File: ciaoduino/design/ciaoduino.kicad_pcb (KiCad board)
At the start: 2 copper layers, 50.5 x 47.8 mm, 19 parts, among them P1 ICSP, P2 CONN_01X02, P3 USB_OTG, P4 CONN_01X06, P5 CONN_01X06, P6 CONN_01X04, P7 CONN_01X14, SW1 SW_PUSH, SW2 SW_PUSH, U2 ATmega32U4-AU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

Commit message: Rework layout.
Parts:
- added REF**: MountingHole_2.5mm, Mounting_Holes:MountingHole_2.5mm, F.Cu at (131.8, 65.8)
- moved P5 5.39 mm to (143.5, 96.5), turned to 270 degrees
- moved P4 5.29 mm to (161.3, 96.5), turned to 90 degrees
- moved P6 4.58 mm to (148.6, 96.5)
- moved P2 2.90 mm to (135.6, 66.8), turned to 90 degrees
- moved REF** 2.70 mm to (172.2, 65.8)
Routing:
- net usart_tx: track 24.9 -> 5.07 mm
- net usart_cts: track 28.3 -> 48.1 mm
- net SCLK: track 25.7 -> 31.2 mm
- net SS: track 29.3 -> 34.4 mm
- net SCL: track 21.3 -> 16.7 mm
- net SDA: track 22.0 -> 17.4 mm
- net GND: track 15.1 -> 16.7 mm
- net VCC: track 145.5 -> 144.5 mm
- net MOSI: track 24.4 -> 23.8 mm
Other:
- board size 50.5 x 47.8 mm -> 50.5 x 42.7 mm

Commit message: Rework layout.
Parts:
- removed REF** (x2): MountingHole_2.5mm, Mounting_Holes:MountingHole_2.5mm
- P4: footprint Pin_Headers:Pin_Header_Angled_1x06 -> Pin_Headers:Pin_Header_Straight_1x06
- SW2: footprint Buttons_Switches_SMD:SW_SPST_EVQP0 -> Buttons_Switches_SMD:SW_SPST_KMR2
- moved P1 41.3 mm to (172.6, 73.0), turned to 0 degrees
- moved SW1 7.19 mm to (164.1, 77.5)
- moved P2 7.08 mm to (128.8, 65.0), turned to 180 degrees
- moved SW2 6.10 mm to (164.2, 73.7)
- moved C3 2.56 mm to (140.2, 76.1), turned to 0 degrees
- moved P6 2.29 mm to (148.6, 98.8)
- moved R4 1.49 mm to (140.2, 72.5)
- moved P3 0.97 mm to (130.4, 75.8)
- moved R3 0.81 mm to (140.2, 74.3)
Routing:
- net VCC: track 144.5 -> 79.9 mm, vias 8 -> 6
- net SS: track 34.4 -> 0.00 mm
- net SCLK: track 31.2 -> 0.64 mm
- net MISO: track 29.6 -> 1.30 mm, vias 2 -> 0
- net MOSI: track 23.8 -> 1.52 mm, vias 1 -> 0
- net usart_cts: track 48.1 -> 28.3 mm
- net RESET: track 49.8 -> 35.6 mm
- net Net-(R2-Pad2): track 17.4 -> 6.26 mm
- net Net-(C3-Pad2): track 8.06 -> 0.00 mm
- net Net-(P3-Pad2): track 6.08 -> 0.24 mm
- net Net-(R4-Pad1): track 5.56 -> 0.00 mm
- net Net-(P3-Pad3): track 5.22 -> 0.00 mm
- net Net-(R3-Pad1): track 5.12 -> 0.00 mm
- net usart_tx: track 5.07 -> 0.00 mm
- net GND: track 16.7 -> 13.9 mm
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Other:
- board size 50.5 x 42.7 mm -> 59.1 x 42.7 mm

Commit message: ciaoduino: rework board.
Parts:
- added C4: C, Capacitors_SMD:C_0603_HandSoldering, F.Cu at (134.4, 63.8)
- added C5: C, Capacitors_SMD:C_0603_HandSoldering, F.Cu at (141.5, 67.8)
- added Q1: Q_NMOS_DGS, TO_SOT_Packages_SMD:SOT-23, F.Cu at (137.9, 67.6)
- added U1: MCP1754ST-5002E/MB, TO_SOT_Packages_SMD:SOT-323, F.Cu at (134.1, 65.8)
- moved R1 6.37 mm to (165.6, 81.3)
- moved P6 4.83 mm to (148.6, 94.0)
- moved C1 3.31 mm to (154.4, 84.8)
- moved C2 3.31 mm to (147.8, 84.8), turned to 90 degrees
- moved X1 2.79 mm to (151.1, 84.8)
- moved P4 2.54 mm to (161.3, 94.0)
- moved P5 2.54 mm to (143.5, 94.0)
- moved R2 0.57 mm to (162.1, 69.6), turned to 270 degrees
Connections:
- P2 pad 2: VCC -> Net-(C4-Pad2)
- P3 pad 1: (no net) -> VCCUSB
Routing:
- net usart_rts: track 38.6 -> 0.00 mm, vias 2 -> 0
- net RESET: track 35.6 -> 4.10 mm, vias 2 -> 0
- net usart_cts: track 28.3 -> 0.00 mm, vias 2 -> 0
- net usart_rx: track 25.1 -> 0.00 mm
- net SDA: track 19.7 -> 0.00 mm
- net SCL: track 19.0 -> 0.00 mm
- net Net-(C4-Pad2): track 0.00 -> 9.40 mm
- net Net-(C2-Pad1): track 14.8 -> 6.34 mm, vias 2 -> 0
- net Net-(C1-Pad1): track 11.5 -> 4.14 mm, vias 2 -> 0
- net Net-(R2-Pad2): track 6.26 -> 12.4 mm
- net GND: track 13.9 -> 17.8 mm
- net VCC: track 79.9 -> 77.0 mm, vias 6 -> 5
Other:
- board size 59.1 x 42.7 mm -> 59.2 x 35.1 mm

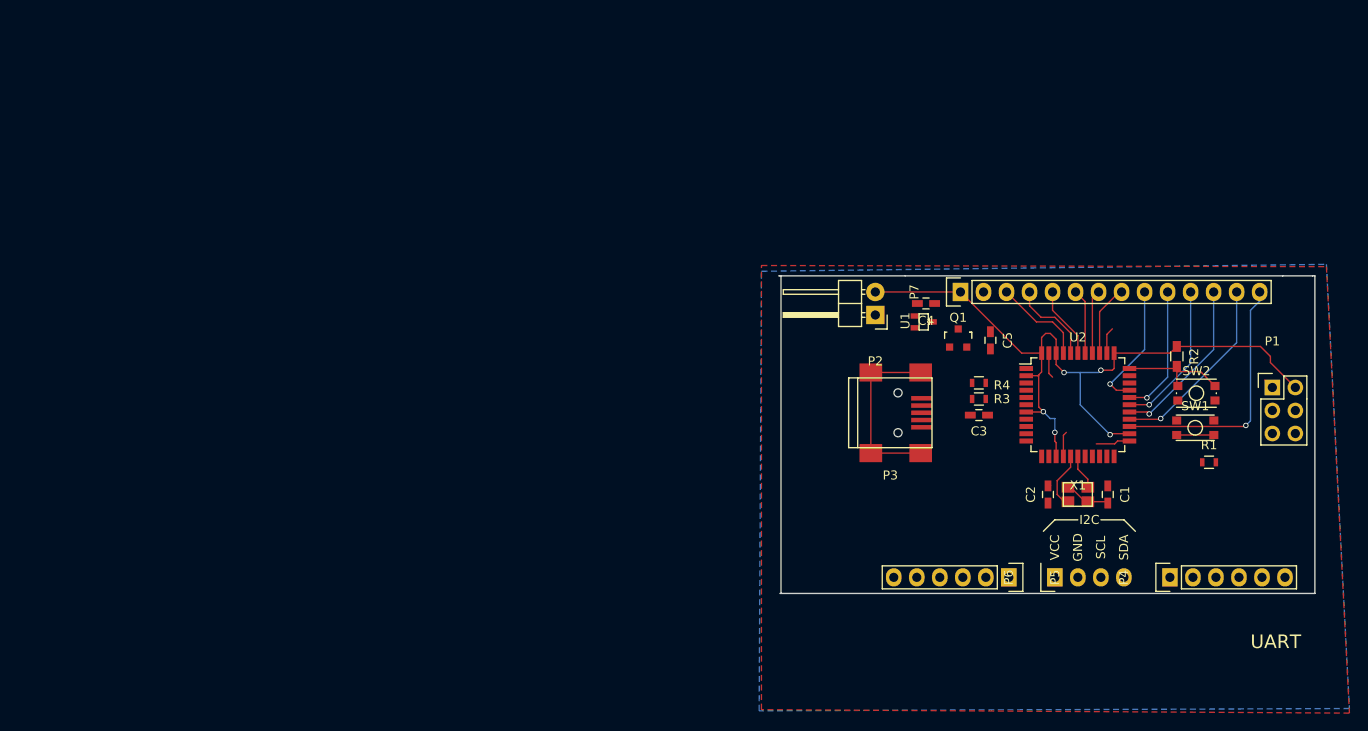
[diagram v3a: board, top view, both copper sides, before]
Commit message: Reorganize pinout.
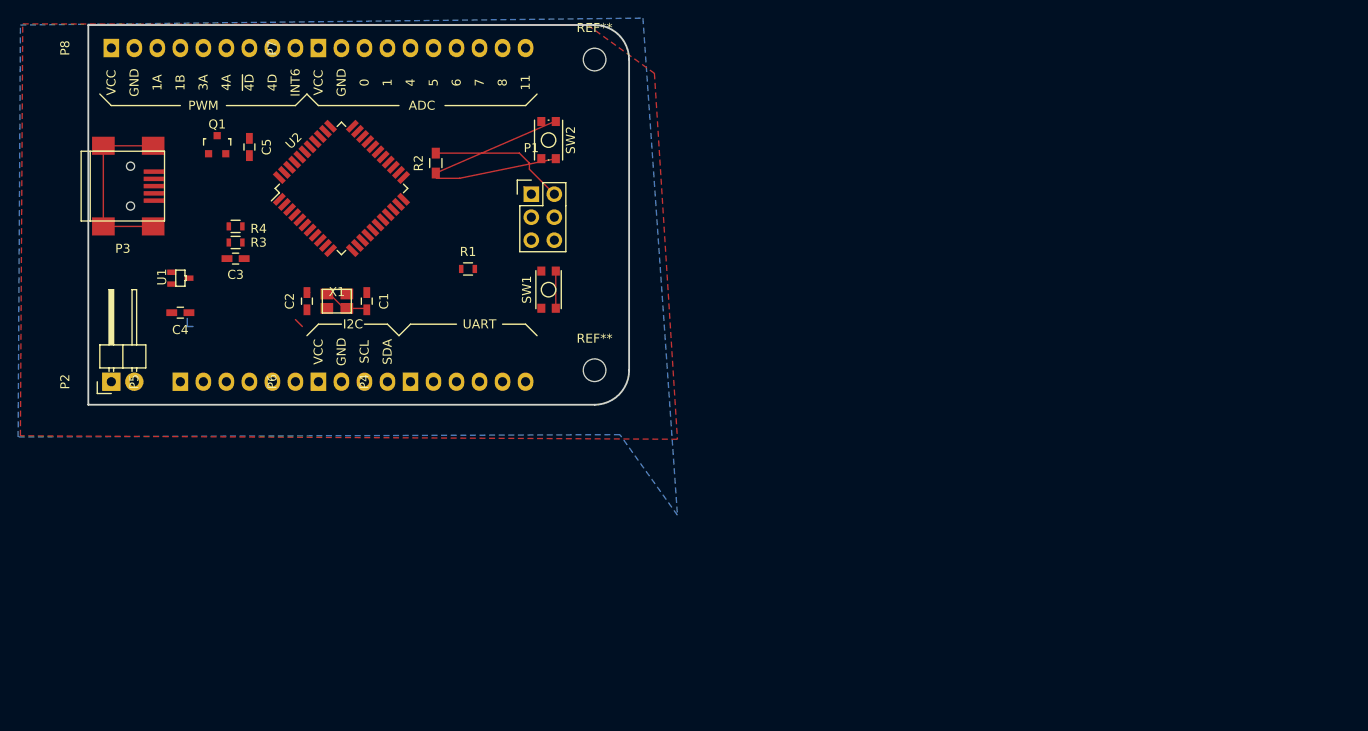
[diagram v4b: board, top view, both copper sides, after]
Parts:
- added P8: CONN_01X07, Pin_Headers:Pin_Header_Straight_1x09, F.Cu at (44.5, 35.6)
- added REF**: MountingHole_5mm, Mounting_Holes:MountingHole_2-5mm, F.Cu at (97.8, 71.1)
- added REF**: MountingHole_5mm, Mounting_Holes:MountingHole_2-5mm, F.Cu at (97.8, 36.8)
- P7: value CONN_01X14 -> CONN_01X10; footprint Pin_Headers:Pin_Header_Straight_1x14 -> Pin_Headers:Pin_Header_Straight_1x10
- moved P5 94.0 mm to (52.1, 72.4), turned to 90 degrees
- moved P3 88.3 mm to (45.7, 50.8)
- moved P4 86.6 mm to (77.5, 72.4)
- moved U2 84.7 mm to (69.8, 51.1), turned to 45 degrees
- moved P2 84.6 mm to (44.5, 72.4), turned to 90 degrees
- moved C5 84.5 mm to (59.7, 46.5)
- moved R1 84.5 mm to (83.8, 59.9)
- moved C2 84.5 mm to (66.0, 63.5)
- moved Q1 84.5 mm to (56.1, 46.2)
- moved R2 84.5 mm to (80.3, 48.3), turned to 90 degrees
- moved X1 84.5 mm to (69.3, 63.5)
- moved C1 84.5 mm to (72.6, 63.5)
- moved P1 84.5 mm to (90.8, 51.7)
- moved P6 84.1 mm to (67.3, 72.4)
- moved C3 83.8 mm to (58.2, 58.8)
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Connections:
- P7 pad 10: ADC12 -> ADC11
- P7 pad 9: ADC13 -> ADC8
- U2 pad 1: (no net) -> INT6
- U2 pad 26: ADC9 -> ~PWM_4D
- U2 pad 27: ADC10 -> PWM_4D
- U2 pad 29: ADC12 -> PWN_1A
- U2 pad 30: ADC13 -> PWN_1B
- U2 pad 31: (no net) -> PWN_3A
- U2 pad 32: (no net) -> PWN_4A
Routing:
- net VCC: track 77.0 -> 22.1 mm, vias 5 -> 0
- net ADC8: track 28.3 -> 0.00 mm, vias 1 -> 0
- net ADC9: track 20.9 -> 0.00 mm, vias 1 -> 0
- net ADC10: track 18.7 -> 0.00 mm, vias 1 -> 0
- net ADC11: track 16.5 -> 0.00 mm, vias 1 -> 0
- net ADC12: track 14.6 -> 0.00 mm, vias 1 -> 0
- net ADC13: track 14.2 -> 0.00 mm, vias 1 -> 0
- net GND: track 17.8 -> 5.45 mm
- net ADC0: track 10.4 -> 0.00 mm
- net ADC1: track 9.52 -> 0.00 mm
- net Net-(C4-Pad2): track 9.40 -> 0.00 mm
- net Net-(R2-Pad2): track 12.4 -> 21.8 mm
- net ADC4: track 7.90 -> 0.00 mm
- net ADC7: track 7.90 -> 0.00 mm
- net ADC5: track 7.18 -> 0.00 mm
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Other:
- board size 59.2 x 35.1 mm -> 59.7 x 41.9 mm
- board text removed: "UART"

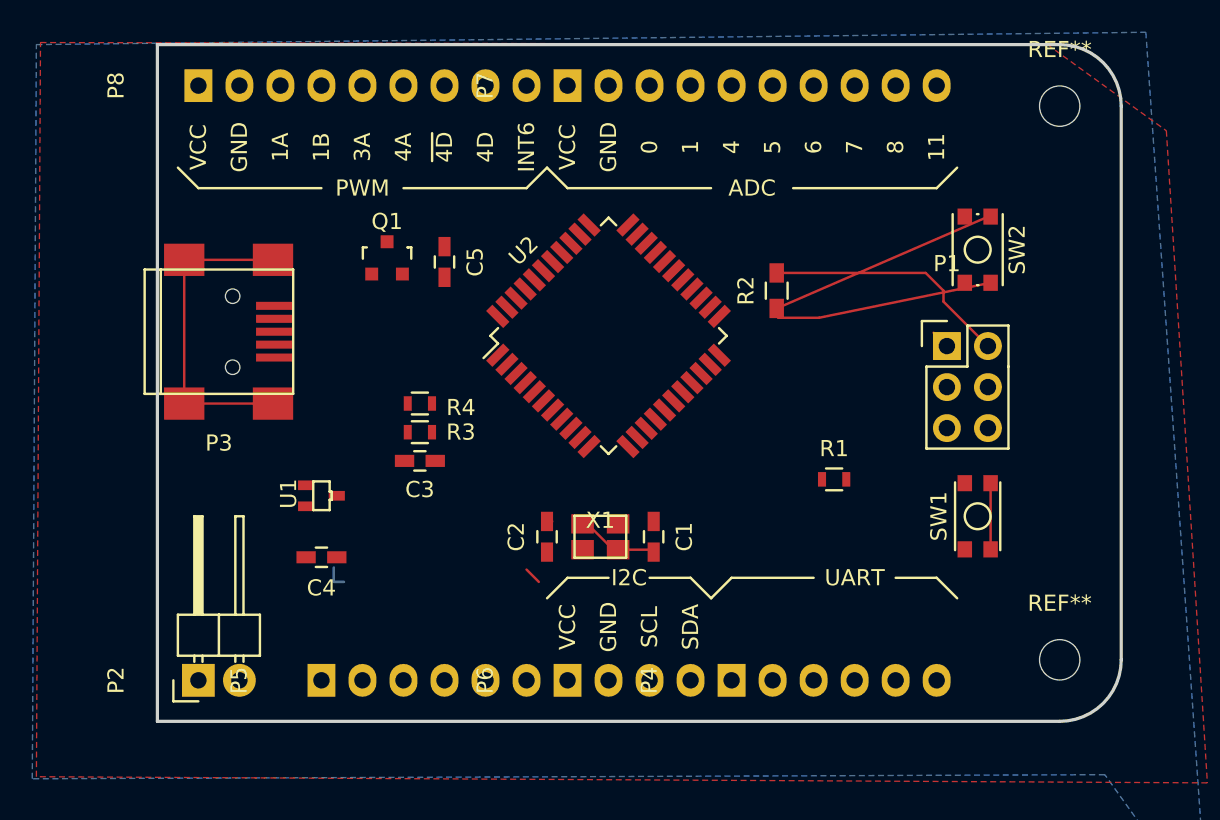
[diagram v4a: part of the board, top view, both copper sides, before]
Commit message: ciaoduino: complete a messy routing.
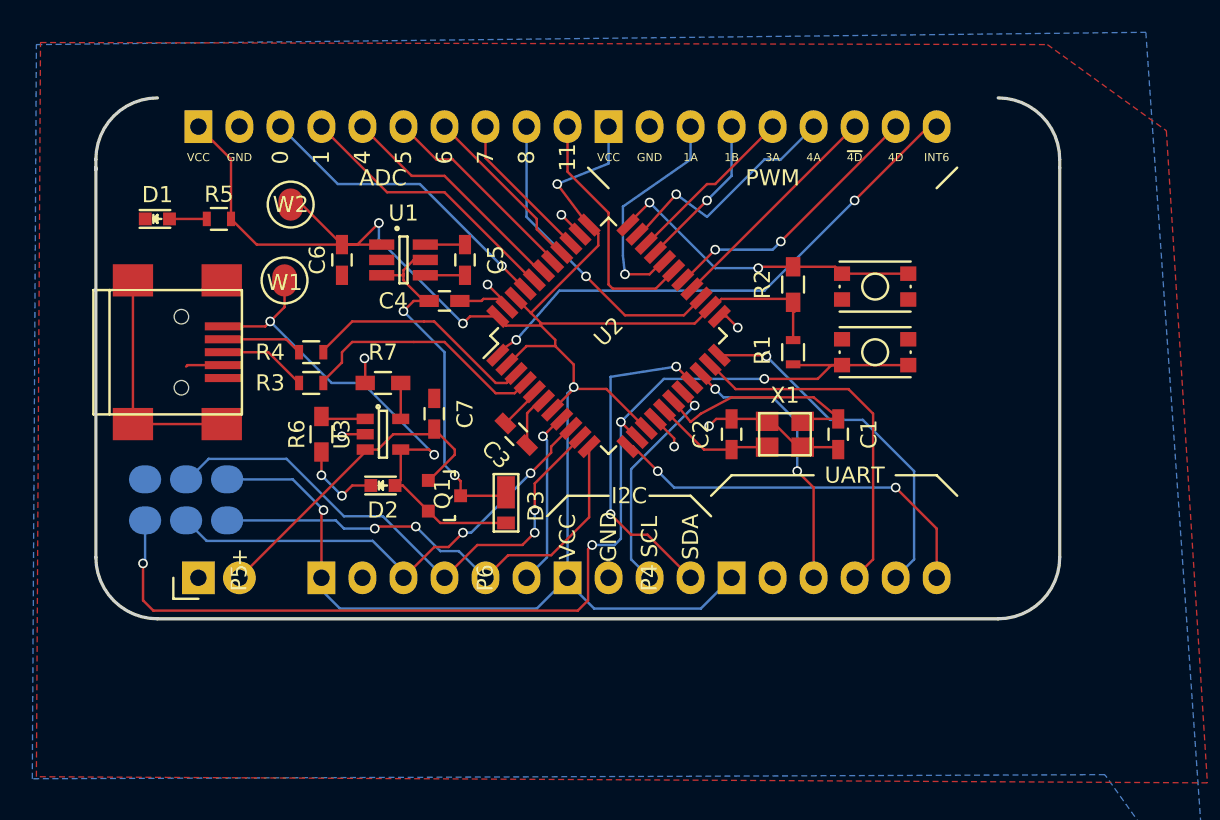
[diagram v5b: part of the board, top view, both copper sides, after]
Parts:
- removed REF** (x2): MountingHole_5mm, Mounting_Holes:MountingHole_2-5mm
- added C6: 1uF, Capacitors_SMD:C_0603_HandSoldering, F.Cu at (53.3, 46.4)
- added C7: 10uF, Capacitors_SMD:C_0603_HandSoldering, F.Cu at (59.1, 55.9)
- added D1: LED, LEDs:LED_0603, F.Cu at (41.9, 43.8)
- added D2: LED, LEDs:LED_0603, F.Cu at (55.9, 60.3)
- added D3: D_Schottky, Diodes_SMD:TUMD2, F.Cu at (63.5, 61.6)
- added R5: R, Resistors_SMD:R_0603, F.Cu at (45.7, 43.8)
- added R6: 1K, Resistors_SMD:R_0603_HandSoldering, F.Cu at (52.1, 57.1)
- added R7: 10K, Resistors_SMD:R_0603_HandSoldering, F.Cu at (55.9, 54.0)
- added U3: MCP73831, TO_SOT_Packages_SMD:SOT-23-5, F.Cu at (55.9, 57.1)
- added W1: TEST_1P, TEST_1Pin, F.Cu at (49.8, 47.6)
- added W2: TEST_1P, ciaoduino:TEST_1Pin, F.Cu at (50.2, 42.9)
- C4, C5: value C -> 1uF
- P1: footprint Pin_Headers:Pin_Header_Straight_2x03 -> ciaoduino:ICSP_SMD; moved to B.Cu
- P7: footprint Pin_Headers:Pin_Header_Straight_1x10 -> Pin_Header_Straight_1x10
- Q1: value Q_NMOS_DGS -> Q_NMOS_SGD
- U1: value MCP1754ST-5002E/MB -> LTC3200-5; footprint TO_SOT_Packages_SMD:SOT-323 -> TO_SOT_Packages_SMD:SOT-23-6_Handsoldering
- moved P1 45.9 mm to (46.2, 62.5), turned to 90 degrees
- moved P8 25.5 mm to (69.8, 38.1)
- moved P7 23.0 mm to (44.5, 38.1)
- moved C4 17.6 mm to (59.7, 48.9), turned to 0 degrees
- moved U1 15.5 mm to (57.1, 46.4), turned to 0 degrees
- moved Q1 15.2 mm to (59.7, 61.0), turned to 270 degrees
- moved X1 13.1 mm to (80.8, 57.1)
- moved C1 13.1 mm to (84.1, 57.1)
- moved C2 13.1 mm to (77.5, 57.1)
- moved SW1 12.0 mm to (86.4, 52.1), turned to 0 degrees
- moved R1 8.27 mm to (81.3, 52.1), turned to 270 degrees
- moved R4 7.44 mm to (51.4, 52.1)
- moved R3 7.39 mm to (51.4, 54.0)
- moved SW2 6.75 mm to (86.4, 48.0), turned to 0 degrees
- moved P2 6.35 mm to (44.5, 66.0)
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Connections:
- C4 pad 1: GND -> VIN
- C4 pad 2: Net-(C4-Pad2) -> GND
- C5 pad 1: GND -> Net-(C5-Pad1)
- C5 pad 2: VIN -> Net-(C5-Pad2)
- P2 pad 2: Net-(C4-Pad2) -> Net-(C7-Pad1)
- P3 pad 4: (no net) -> GND
- P3 pad 6: Net-(P3-Pad6) -> GND
- Q1 pad 1: VCCUSB -> Net-(C7-Pad1)
- Q1 pad 2: VIN -> VCCUSB
- Q1 pad 3: VCC -> VIN
- U1 pad 1: Net-(C4-Pad2) -> VCC
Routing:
- net VCC: track 22.1 -> 143.1 mm, vias 0 -> 5
- net RESET: track 4.10 -> 69.5 mm, vias 0 -> 4
- net GND: track 5.45 -> 42.1 mm, vias 0 -> 7
- net MOSI: track 0.00 -> 33.4 mm, vias 0 -> 2
- net INT6: track 0.00 -> 33.2 mm, vias 0 -> 2
- net VCCUSB: track 0.00 -> 32.6 mm, vias 0 -> 2
- net SCLK: track 0.00 -> 29.6 mm, vias 0 -> 2
- net MISO: track 1.30 -> 29.9 mm, vias 0 -> 2
- net usart_rts: track 0.00 -> 24.3 mm, vias 0 -> 2
- net VIN: track 0.00 -> 23.4 mm, vias 0 -> 2
- net usart_cts: track 0.00 -> 22.1 mm, vias 0 -> 1
- net usart_tx: track 0.00 -> 22.0 mm
- net SDA: track 0.00 -> 20.6 mm, vias 0 -> 2
- net Net-(C7-Pad1): track 0.00 -> 20.4 mm
- net Net-(P3-Pad6): track 19.9 -> 0.00 mm
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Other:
- board size 59.7 x 41.9 mm -> 59.7 x 32.3 mm
- board text added: "CIAODUINO Board Vin: 12-7V Vcc: 5V Pins are 5V tollerant"
